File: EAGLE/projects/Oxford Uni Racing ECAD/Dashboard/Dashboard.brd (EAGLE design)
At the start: 160 x 139.4 mm, 3 parts, among them J1 T821108A1S100CEU, K1 EC2-12NU, K2 EC2-12NU

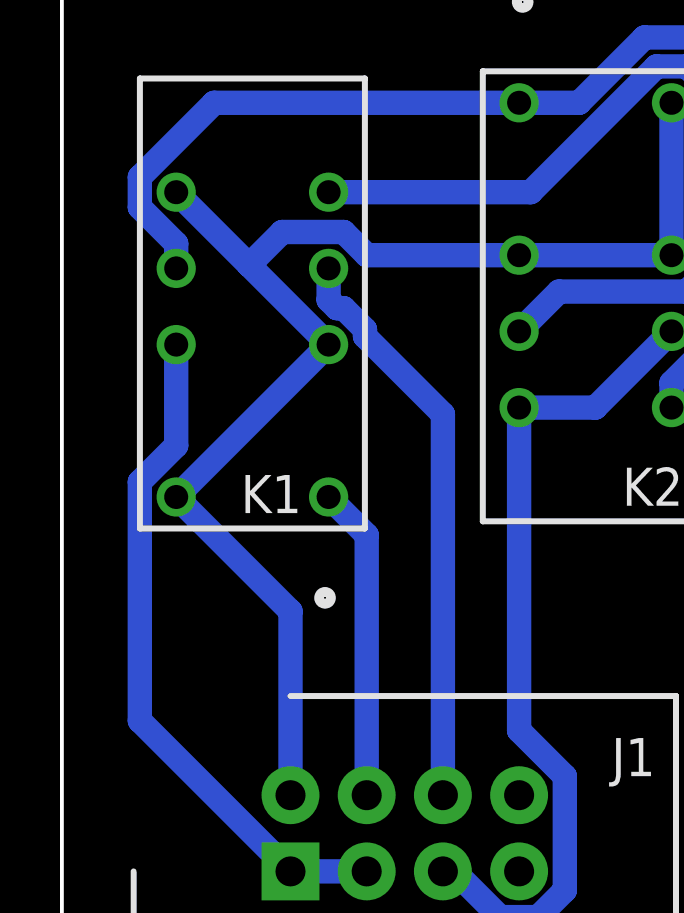
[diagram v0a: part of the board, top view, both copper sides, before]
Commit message: added cross sheet connections to dashboard
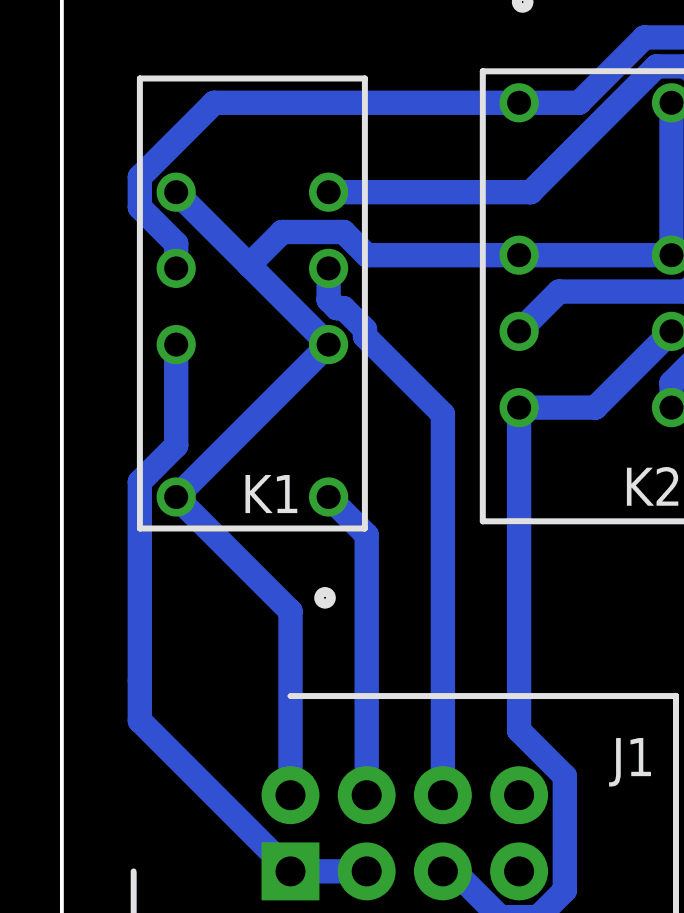
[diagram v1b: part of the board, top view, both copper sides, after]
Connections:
- net +12V renamed 12V

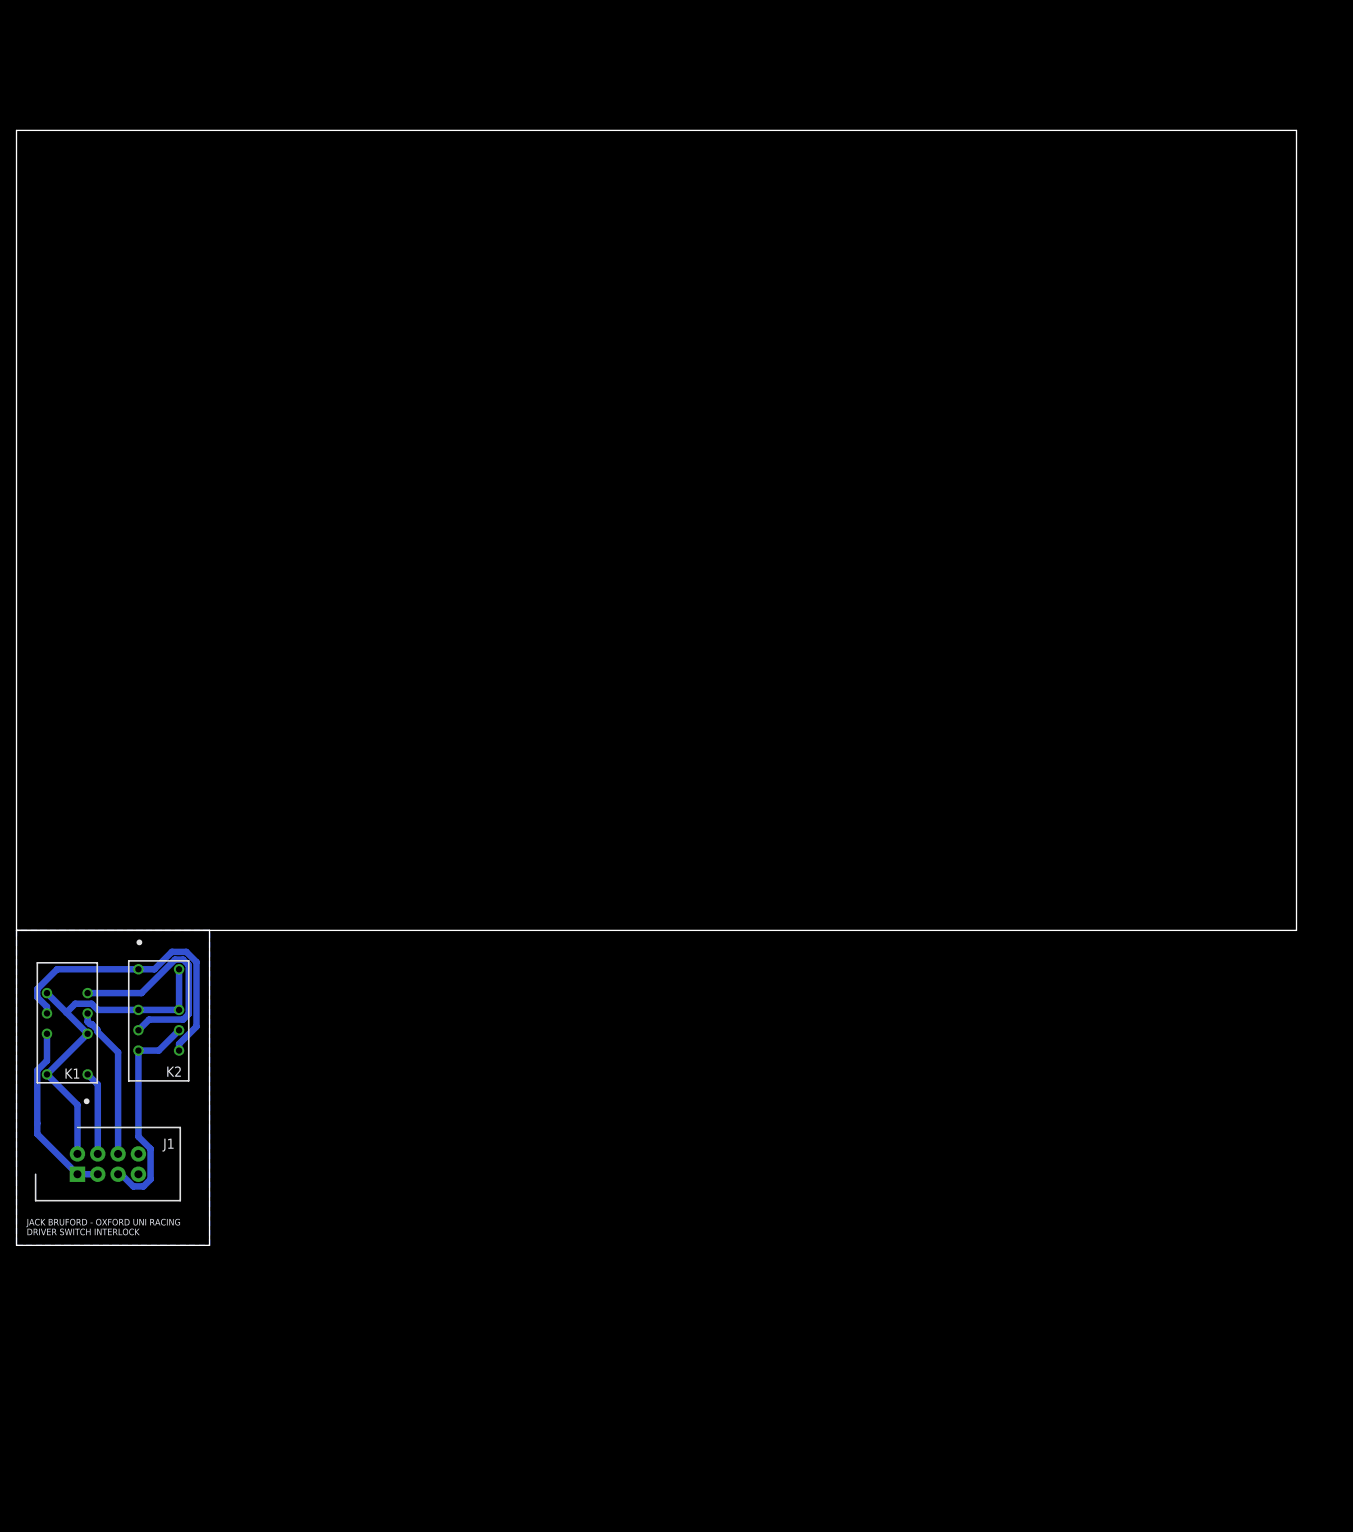
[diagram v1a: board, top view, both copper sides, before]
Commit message: removed throttle position sensor 3 from all chematics
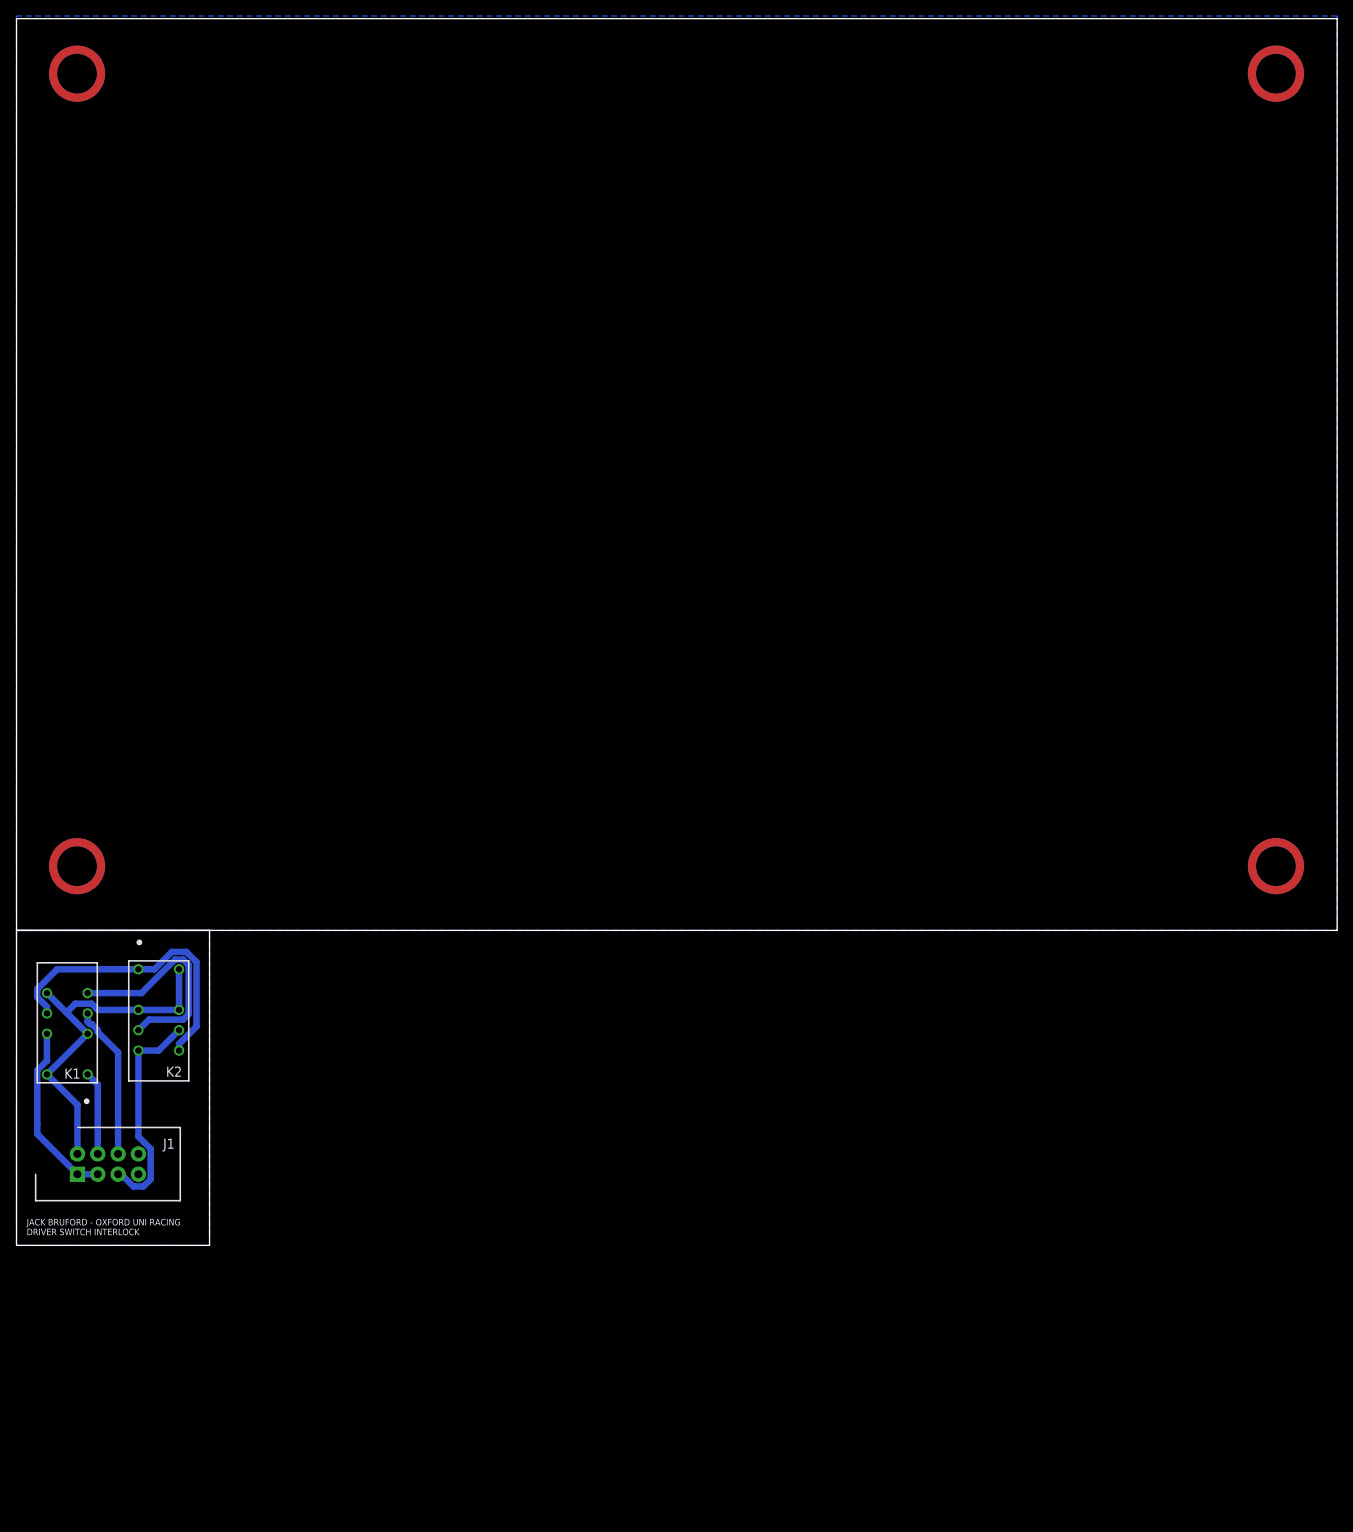
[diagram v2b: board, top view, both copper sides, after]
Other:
- board size 160 x 139.4 mm -> 165.1 x 153.3 mm
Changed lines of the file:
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@@
 <board>
 <plain>
-<wire x1="0" y1="0" x2="160" y2="0" width="0" layer="20"/>
-<wire x1="160" y1="0" x2="160" y2="100" width="0" layer="20"/>
-<wire x1="160" y1="100" x2="0" y2="100" width="0" layer="20"/>
-<wire x1="0" y1="100" x2="0" y2="0" width="0" layer="20"/>
+<wire x1="0" y1="0" x2="165.08" y2="0" width="0" layer="20"/>
+<wire x1="165.08" y1="0" x2="165.08" y2="113.97" width="0" layer="20"/>
+<wire x1="165.08" y1="113.97" x2="0" y2="113.97" width="0" layer="20"/>
+<wire x1="0" y1="113.97" x2="0" y2="0" width="0" layer="20"/>
 <wire x1="0" y1="-39.37" x2="0" y2="0" width="0.127" layer="20"/>
 <wire x1="24.13" y1="0" x2="24.13" y2="-39.37" width="0.127" layer="20"/>
@@
 <text x="1.27" y="-38.1" size="0.8128" layer="21">JACK BRUFORD - OXFORD UNI RACING
 DRIVER SWITCH INTERLOCK</text>
+<wire x1="0" y1="0" x2="165.1" y2="0" width="0.1524" layer="49"/>
+<wire x1="165.1" y1="0" x2="165.1" y2="114.3" width="0.1524" layer="49"/>
+<wire x1="165.1" y1="114.3" x2="0" y2="114.3" width="0.1524" layer="49"/>
+<wire x1="0" y1="114.3" x2="0" y2="0" width="0.1524" layer="49"/>
+<circle x="7.57" y="107.09" locked="yes" radius="3" width="1.016" layer="16"/>
+<circle x="157.43" y="107.09" locked="yes" radius="3" width="1.016" layer="16"/>
+<circle x="7.57" y="8.03" locked="yes" radius="3" width="1.016" layer="16"/>
+<circle x="157.43" y="8.03" locked="yes" radius="3" width="1.016" layer="16"/>
+<circle x="7.57" y="107.09" locked="yes" radius="3" width="1.016" layer="1"/>
+<circle x="157.43" y="107.09" locked="yes" radius="3" width="1.016" layer="1"/>
+<circle x="157.43" y="8.03" locked="yes" radius="3" width="1.016" layer="1"/>
+<circle x="7.57" y="8.03" locked="yes" radius="3" width="1.016" layer="1"/>
 </plain>
 <attributes>
@@
 <wire x1="7.62" y1="-21.81" x2="7.62" y2="-27.94" width="0.8128" layer="16"/>
 <wire x1="15.24" y1="-9.94" x2="20.32" y2="-9.94" width="0.8128" layer="16"/>
+<polygon width="0.1524" layer="16" isolate="0.3048" locked="yes">
+<vertex x="0" y="114.3"/>
+<vertex x="0" y="0"/>
+<vertex x="165.1" y="0"/>
+<vertex x="165.1" y="114.3"/>
+</polygon>
 </signal>
 <signal name="DRIVERSWITCH-">
@@
 which will not be processed correctly with this version.
 </note>
+<note version="8.5" severity="warning">
+Since Version 8.5, EAGLE supports locking for holes, vias, wires and polygons.
+The locking property on all objects of these types will not be understood in this version.
+</note>
 </compatibility>
